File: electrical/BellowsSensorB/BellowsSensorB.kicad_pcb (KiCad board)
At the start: 2 copper layers, 32 x 20 mm, 5 parts, among them J1 I2C, U1 CPS610DSD010DH01

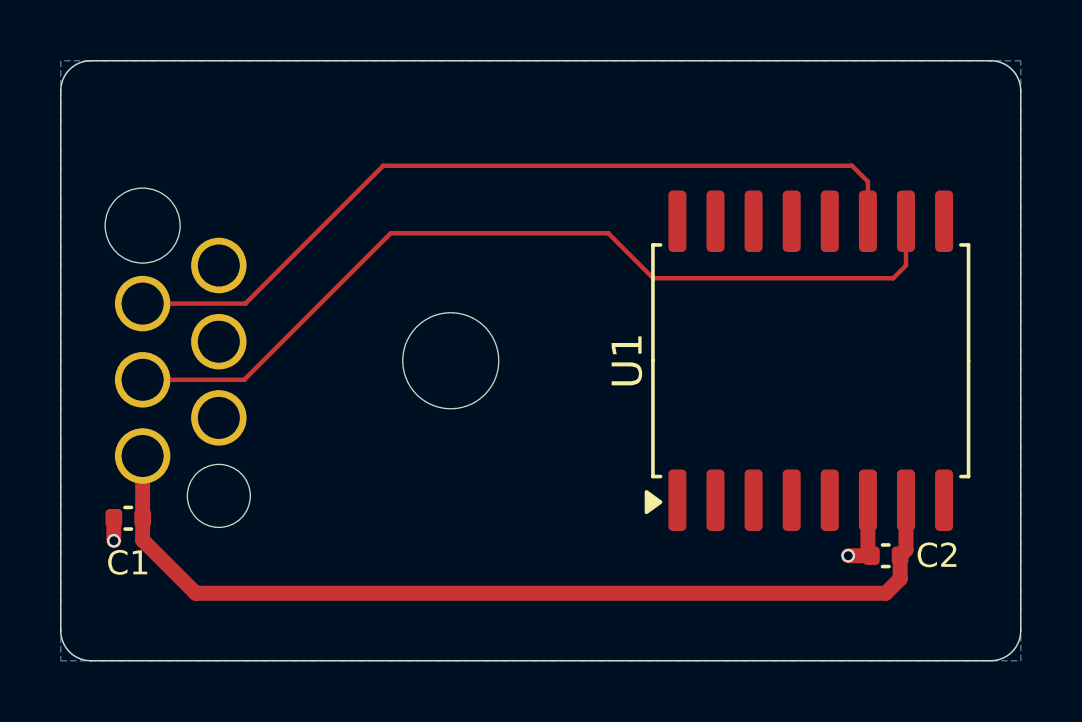
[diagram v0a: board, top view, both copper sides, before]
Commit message: Switch pressure sensor for BellowsSensorB
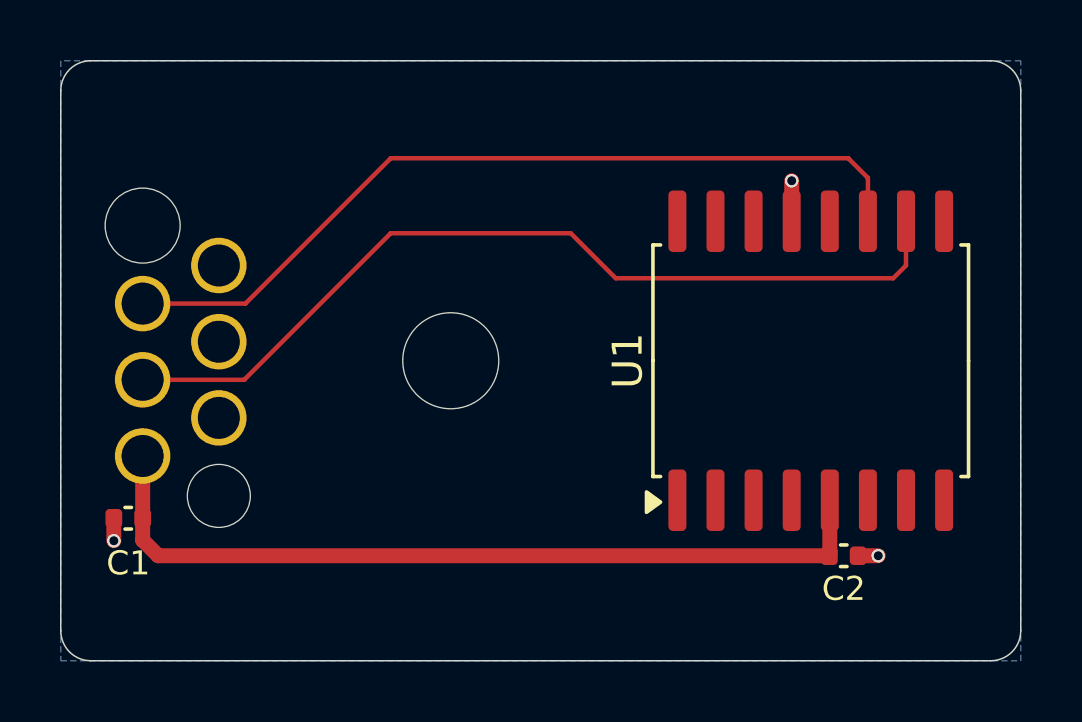
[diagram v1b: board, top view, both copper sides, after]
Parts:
- U1: value CPS610DSD010DH01 -> WF200DPZ 0.1BG S16 DT
- moved C2 1.40 mm to (154.1, 110.5), turned to 0 degrees
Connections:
- U1 pad 13: unconnected-(U1-Pad13) -> GND
- U1 pad 5: unconnected-(U1-Pad5) -> +3.3V
- U1 pad 6: GND -> unconnected-(U1-INT-Pad6)
- U1 pad 7: +3.3V -> unconnected-(U1-CS-Pad7)
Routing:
- net +3.3V: track 31.7 -> 27.8 mm
- net GND: track 3.42 -> 2.77 mm, vias 2 -> 3
